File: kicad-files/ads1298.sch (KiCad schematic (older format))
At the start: 56 parts, among them J10 Conn_01x01, J11 Conn_01x01, J2 Conn_01x01, J3 Conn_01x01, J4 Conn_01x01, J5 Conn_01x01, J6 Conn_01x01, J7 Conn_01x01, J8 Conn_01x01, J9 Conn_01x01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

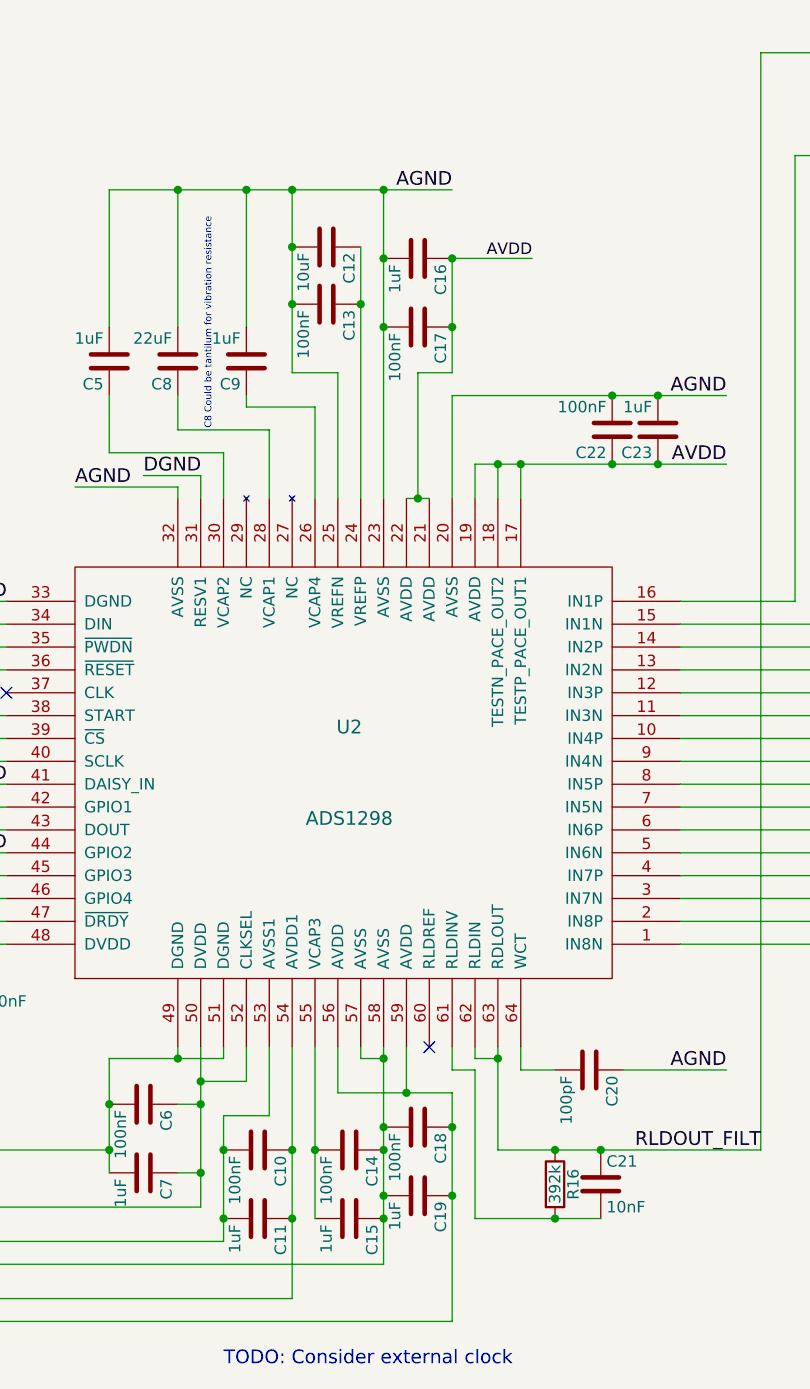
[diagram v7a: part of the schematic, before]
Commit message: eliminate old notes from schematic or move to notes.txt
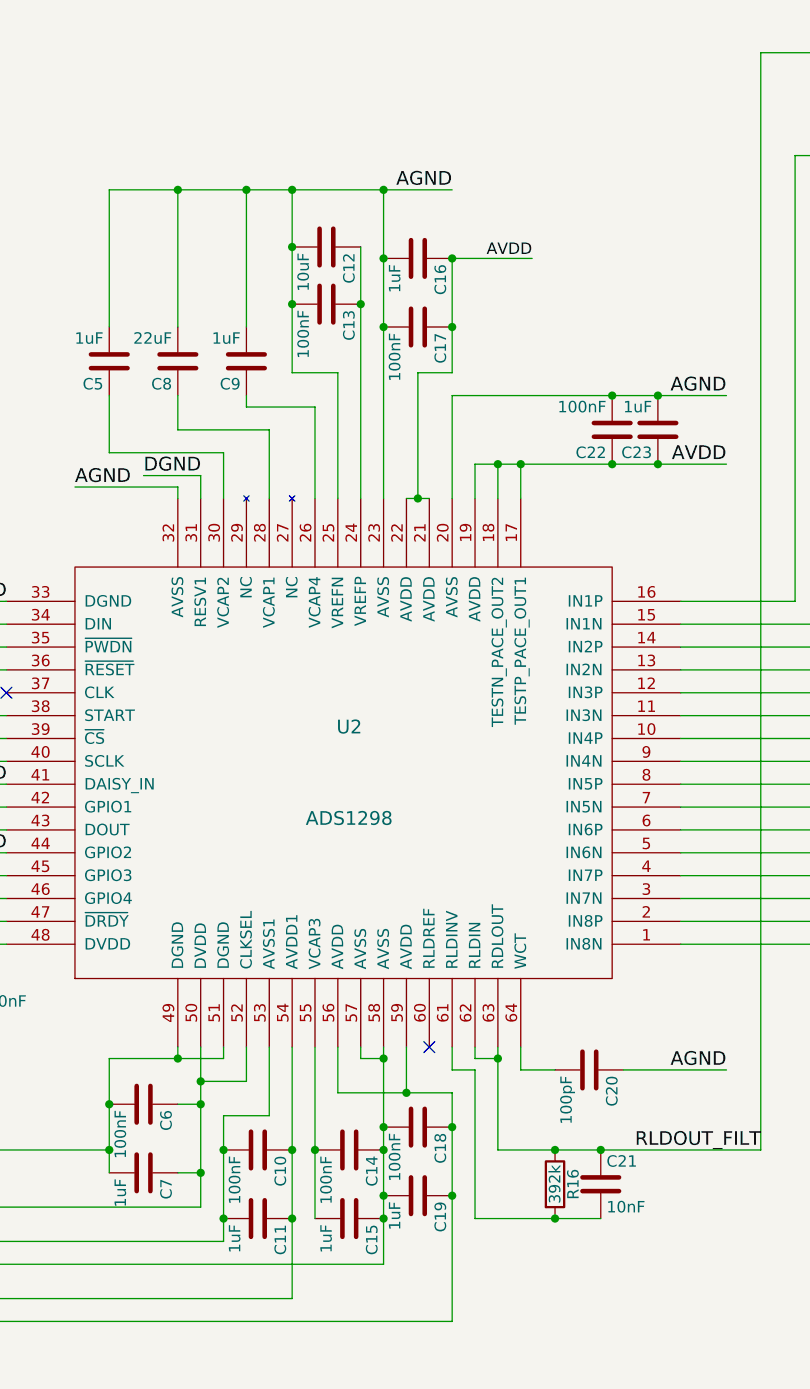
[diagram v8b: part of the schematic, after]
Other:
- note removed: "C8 Could be tantilum for vibration resistance"
- note removed: "TODO: Consider external clock"
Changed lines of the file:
@@
 chest
 Connection ~ 7500 3100
-Text Notes 4800 6350 0    60   ~ 0
-TODO: Consider external clock
 $Comp
 L OpenHardwareHolterMonitor-rescue:Conn_01x01 J2
@@
 	1    0    0    -1
 $EndComp
-Text Notes 4750 2250 1    30   ~ 0
-C8 Could be tantilum for vibration resistance
 Wire Wire Line
 	4600 5000 4800 5000
